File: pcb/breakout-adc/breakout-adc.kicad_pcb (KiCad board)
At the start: 4 copper layers, 100 x 62 mm, 107 parts, among them J1 Screw_Terminal_01x04, J10 Conn_01x01_Pin, J11 Conn_01x12_Pin, J12 Conn_01x12_Pin, J13 Conn_01x01_Pin, J14 Conn_01x01_Pin, J15 FX18-120P-0.8SV20, J16 Conn_01x01_Pin, J17 Conn_01x01_Pin, J18 Conn_01x01_Pin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

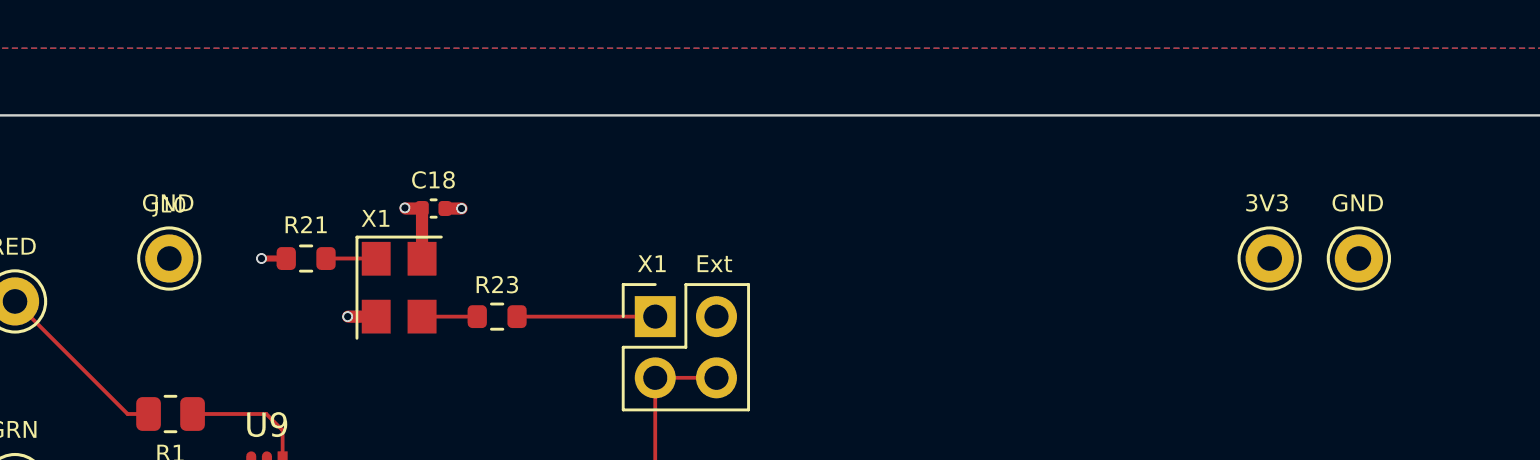
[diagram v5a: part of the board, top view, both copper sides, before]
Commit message: [adc][pcb] move the 3v3 and gnd tp to the edge
This will (probably) allow for grabbers to connect
to the through holes even if the tp isn't soldered in.
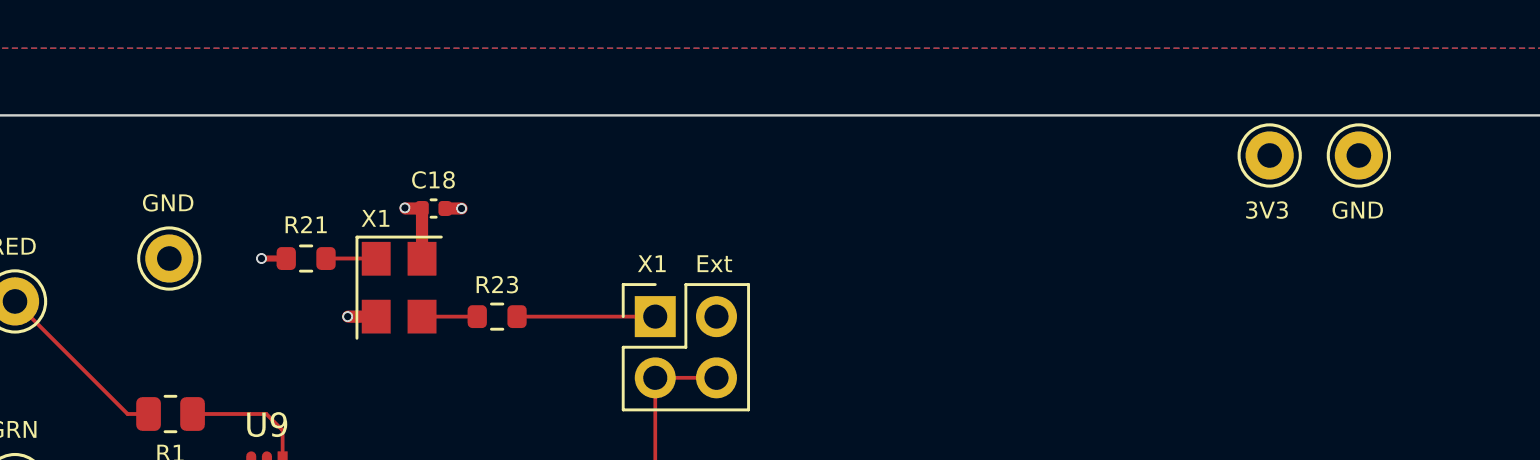
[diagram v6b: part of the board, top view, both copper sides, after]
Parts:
- moved J13 4.27 mm to (176.3, 45.2)
- moved J14 4.27 mm to (180.1, 45.2)
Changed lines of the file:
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@@
 	(footprint "keystone:KEYSTONE_5000"
 		(layer "F.Cu")
-		(at 176.35 49.475)
+		(at 176.35 45.2)
 		(property "Reference" "J13"
 			(at 0.032 -2.2064 0)
@@
 			(at 0.032 -2.2064 0)
 			(layer "F.SilkS")
+			(hide yes)
 			(effects
 				(font
@@
 	(footprint "keystone:KEYSTONE_5001"
 		(layer "F.Cu")
-		(at 180.05 49.475)
+		(at 180.05 45.2)
 		(property "Reference" "J14"
 			(at 0.032 -2.2064 0)
@@
 	)
 	(gr_text "GND"
-		(at 178.903334 47.6 0)
+		(at 178.903334 47.9 0)
 		(layer "F.SilkS")
 		(effects
@@
 	)
 	(gr_text "3V3"
-		(at 175.303333 47.6 0)
+		(at 175.303333 47.9 0)
 		(layer "F.SilkS")
 		(effects

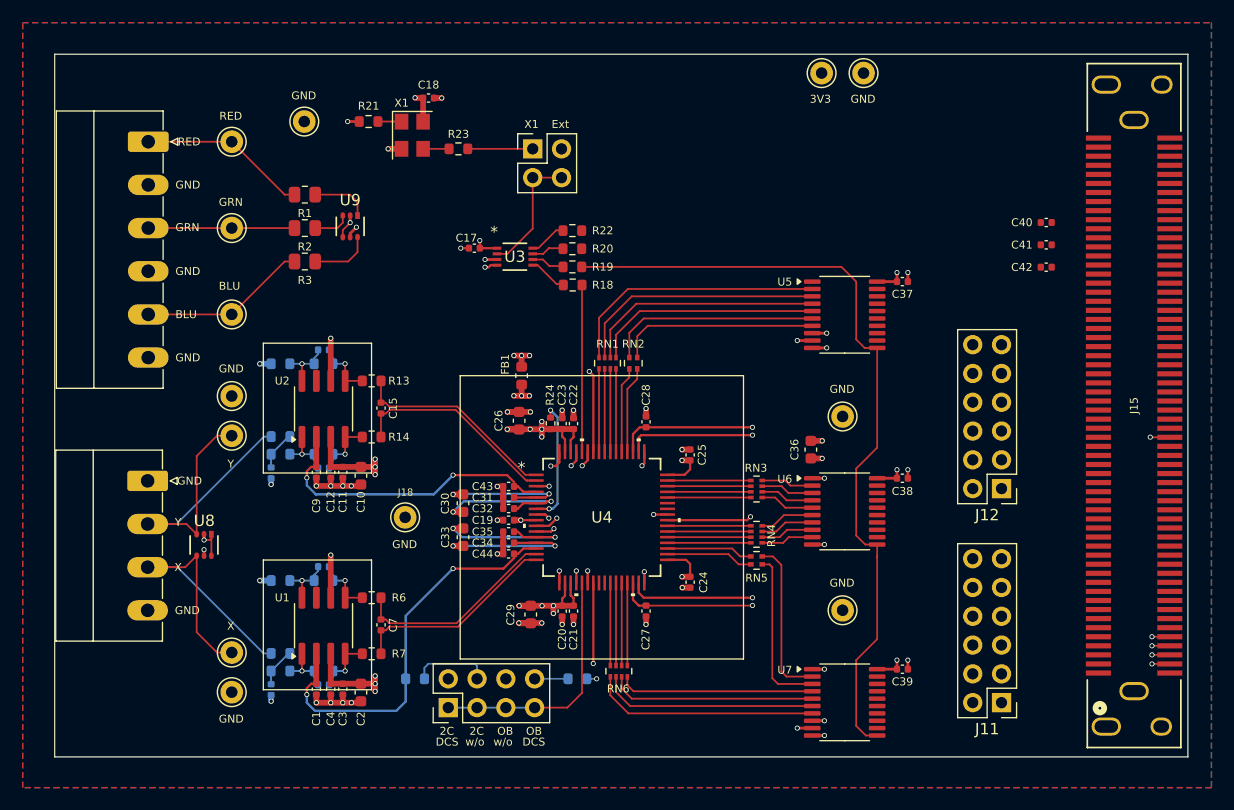
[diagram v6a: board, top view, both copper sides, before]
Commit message: [adc][pcb] routed data to buffers
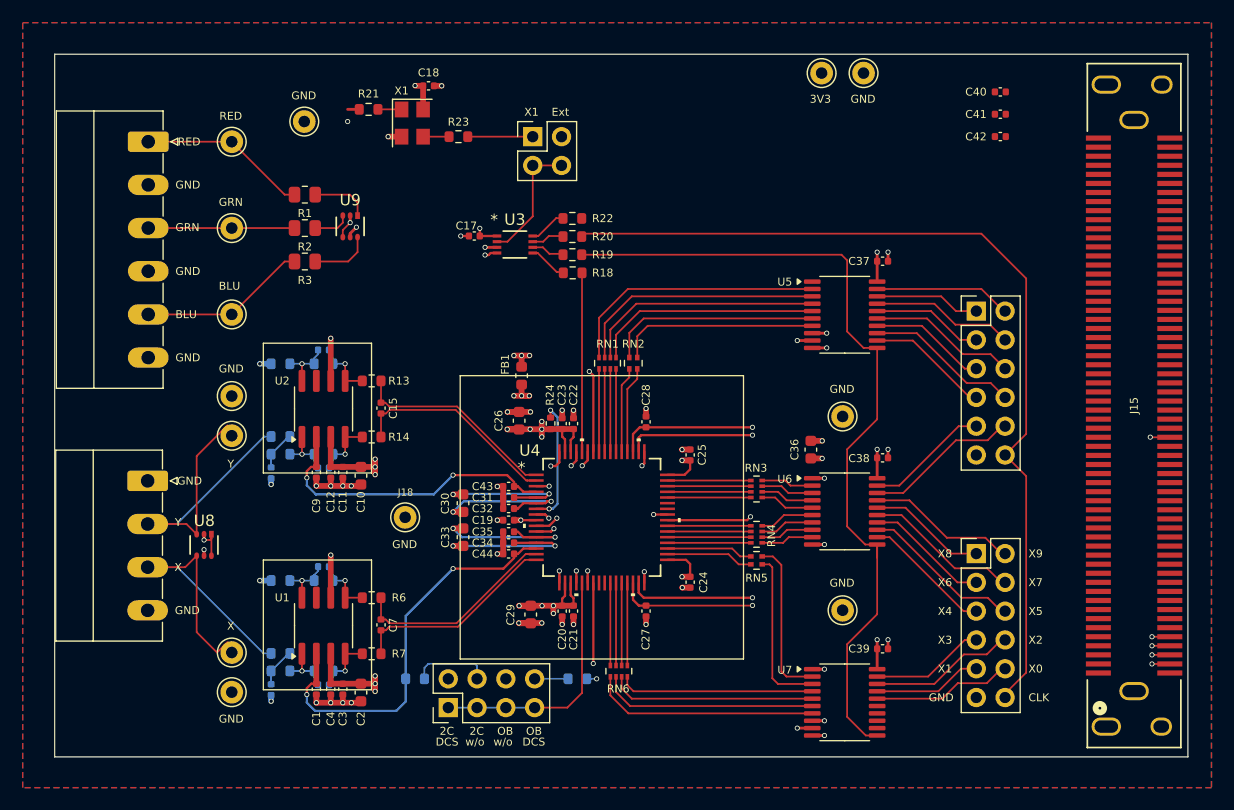
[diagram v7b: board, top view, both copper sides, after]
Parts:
- moved J12 15.8 mm to (190.0, 66.2), turned to 0 degrees
- moved J11 13.3 mm to (190.0, 87.6), turned to 0 degrees
- moved C42 12.2 mm to (192.1, 50.8)
- moved C40 12.2 mm to (192.1, 46.9)
- moved C41 12.2 mm to (192.1, 48.8)
- moved C37 2.51 mm to (181.7, 61.8)
- moved C38 2.51 mm to (181.7, 79.2)
- moved C39 2.51 mm to (181.7, 96.0)
- moved C17 1.08 mm to (145.7, 59.6)
- moved R20 1.08 mm to (154.4, 59.6)
- moved R21 1.08 mm to (136.4, 48.4)
- moved R22 1.08 mm to (154.4, 58.0)
- moved R23 1.08 mm to (144.3, 50.8)
- moved C18 1.07 mm to (141.7, 46.3)
- moved J20 1.07 mm to (150.9, 50.8)
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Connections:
- J11 pad 1: /X0 -> /X8
- J11 pad 10: /X9 -> /X0
- J11 pad 11: /ADC_CLK_HDR -> GND
- J11 pad 12: GND -> /ADC_CLK_HDR
- J11 pad 2: /X1 -> /X9
- J11 pad 3: /X2 -> /X6
- J11 pad 4: /X3 -> /X7
- J11 pad 7: /X6 -> /X3
- J11 pad 8: /X7 -> /X2
- J11 pad 9: /X8 -> /X1
- J12 pad 1: /Y0 -> /Y8
- J12 pad 10: /Y9 -> /Y0
- J12 pad 11: /ADC_CLK_HDR -> GND
- J12 pad 12: GND -> /ADC_CLK_HDR
- J12 pad 2: /Y1 -> /Y9
- J12 pad 3: /Y2 -> /Y6
- J12 pad 4: /Y3 -> /Y7
- J12 pad 7: /Y6 -> /Y2
- J12 pad 8: /Y7 -> /Y3
- J12 pad 9: /Y8 -> /Y1
- J3 pad 1: (no net) -> /X
- J4 pad 1: (no net) -> /Y
- R20 pad 1: /ADC_CLK_FPGA -> /ADC_CLK_HDR
- R22 pad 1: /ADC_CLK_HDR -> /ADC_CLK_FPGA
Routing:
- net /ADC_CLK_HDR: track 0.00 -> 80.4 mm
- net /X5: track 0.00 -> 13.9 mm
- net /Y0: track 0.00 -> 13.7 mm
- net /Y3: track 0.00 -> 13.6 mm
- net /X7: track 0.00 -> 13.4 mm
- net /X9: track 0.00 -> 13.2 mm
- net /Y5: track 0.00 -> 13.1 mm
- net /X2: track 0.00 -> 12.9 mm
- net /Y7: track 1.59 -> 14.2 mm
- net /Y9: track 1.66 -> 13.8 mm
- net /X0: track 0.00 -> 12.0 mm
- net /X4: track 0.00 -> 11.1 mm
- net /Y1: track 0.00 -> 10.9 mm
- net /Y2: track 0.00 -> 10.8 mm
- net /X6: track 0.00 -> 10.6 mm
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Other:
- board text added: "CLK"
- board text added: "X0"
- board text added: "X2"
- board text added: "X3"
- board text added: "X4"
- board text added: "X5"
- board text added: "X6"
- board text added: "X7"
- board text added: "X8"
- board text added: "X9"

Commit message: [pcb] add FX18-120P footprint and update pcbs
and a few adc fixes, including a key resistor fix
(the op amp for Y had a copy paste error from X
on the positive Rg)
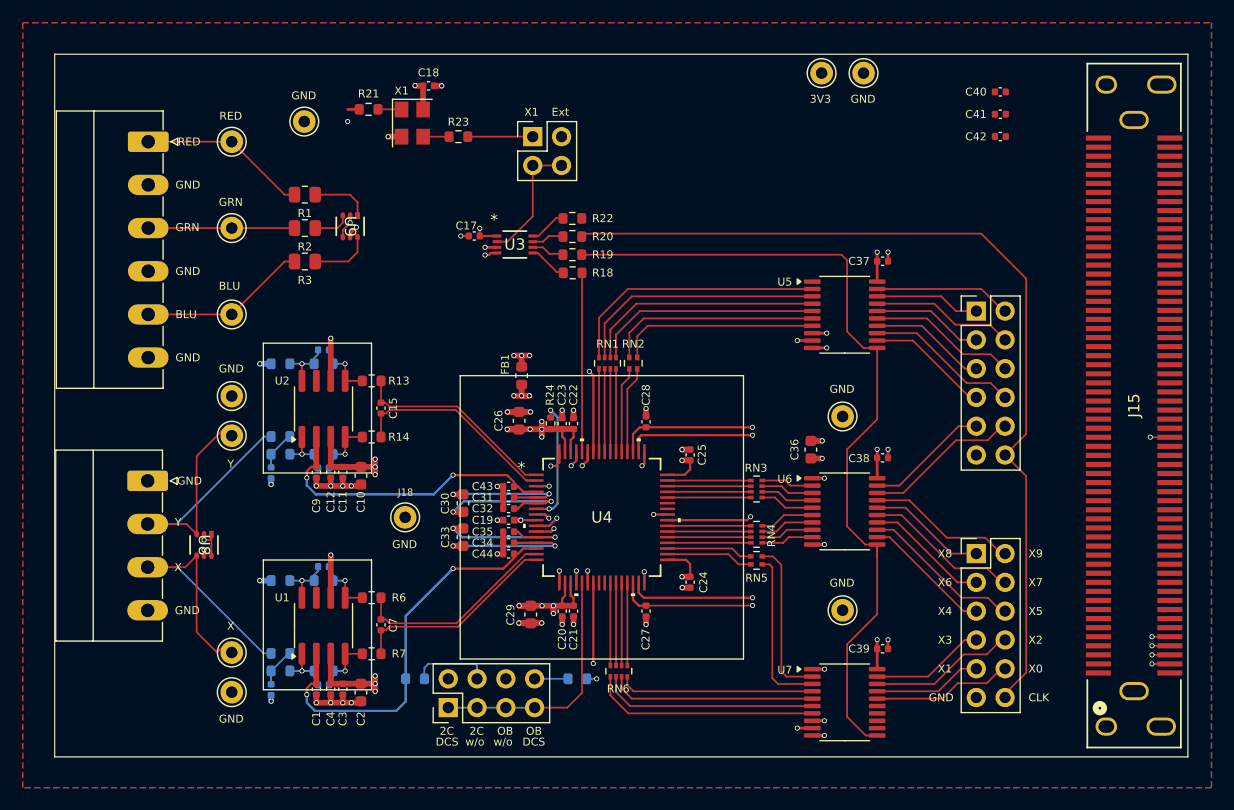
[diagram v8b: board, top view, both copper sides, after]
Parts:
- J15: footprint custom:CUSTOM_FX_120S-0.8SH20 -> custom:CUSTOM_FX_120P-0.8SH20
- R12: value 2.4k -> 1.8k
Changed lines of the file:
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@@
 		(tags "ADC10DL065CIVS/NOPB ")
 		(property "Reference" "U4"
-			(at -6.356666 -5.9 0)
+			(at 0 0 0)
 			(unlocked yes)
 			(layer "F.SilkS")
@@
 			)
 		)
-		(property "Footprint" "ADC10DL065:VEC64A_TEX"
+		(property "Footprint" "VEC64A_TEX"
 			(at 0 0 0)
 			(layer "F.Fab")
@@
 		(fp_text user "*"
 			(at -7.0866 -4.381 0)
-			(unlocked yes)
 			(layer "F.SilkS")
 			(effects
@@
 			)
 		)
-		(fp_text user "${REFERENCE}"
-			(at 0 0 0)
+		(fp_text user "*"
+			(at -4.6228 -3.619 0)
 			(unlocked yes)
 			(layer "F.Fab")
@@
 			)
 		)
-		(fp_text user "*"
-			(at -4.6228 -3.619 0)
+		(fp_text user "${REFERENCE}"
+			(at 0 0 0)
+			(unlocked yes)
 			(layer "F.Fab")
 			(effects
@@
 		(tags "Through hole pin header THT 2x06 2.54mm double row")
 		(property "Reference" "J11"
-			(at 1.27 -2.33 360)
+			(at 1.27 -2.33 0)
 			(layer "F.SilkS")
 			(hide yes)
@@
 		)
 		(property "Value" "Conn_01x12_Pin"
-			(at 1.270001 15.03 360)
+			(at 1.270001 15.03 0)
 			(layer "F.Fab")
 			(effects
@@
 			)
 		)
-		(property "Datasheet" "https://www.ti.com/lit/ds/scas301r/scas301r.pdf"
+		(property "Datasheet" "https://www.ti.com/lit/ds/symlink/sn74als574b.pdf"
 			(at 0 0 0)
 			(unlocked yes)
@@
 		(tags "D1213A-04S-7 ")
 		(property "Reference" "U8"
-			(at -2.14 -0.020491 0)
+			(at 0 0 -90)
 			(unlocked yes)
 			(layer "F.SilkS")
@@
 			)
 		)
-		(property "Footprint" "D1213A:SOT-363_DIO"
-			(at 0 0 90)
+		(property "Footprint" "SOT-363_DIO"
+			(at 0 0 -90)
 			(layer "F.Fab")
 			(hide yes)
@@
 			)
 		)
-		(property "Datasheet" "https://www.diodes.com/assets/Datasheets/D1213A-04S.pdf"
-			(at 0 0 90)
+		(property "Datasheet" "D1213A-04S-7"
+			(at 0 0 -90)
 			(layer "F.Fab")
 			(hide yes)
@@
 		)
 		(property "Description" ""
-			(at 0 0 90)
+			(at 0 0 -90)
 			(layer "F.Fab")
 			(hide yes)
@@
 			)
 		)
-		(property "Datasheet" "https://www.ti.com/lit/ds/scas301r/scas301r.pdf"
+		(property "Datasheet" "https://www.ti.com/lit/ds/symlink/sn74als574b.pdf"
 			(at 0 0 0)
 			(unlocked yes)
@@
 			)
 		)
-		(property "Datasheet" "https://www.ti.com/lit/ds/scas301r/scas301r.pdf"
+		(property "Datasheet" "https://www.ti.com/lit/ds/symlink/sn74als574b.pdf"
 			(at 0 0 0)
 			(unlocked yes)
@@
 		(tags "D1213A-04S-7 ")
 		(property "Reference" "U9"
-			(at -2.325 0 0)
+			(at 0 0 -90)
 			(unlocked yes)
 			(layer "F.SilkS")
@@
 			)
 		)
-		(property "Footprint" "D1213A:SOT-363_DIO"
-			(at 0 0 90)
+		(property "Footprint" "SOT-363_DIO"
+			(at 0 0 -90)
 			(layer "F.Fab")
 			(hide yes)
@@
 			)
 		)
-		(property "Datasheet" "https://www.diodes.com/assets/Datasheets/D1213A-04S.pdf"
-			(at 0 0 90)
+		(property "Datasheet" "D1213A-04S-7"
+			(at 0 0 -90)
 			(layer "F.Fab")
 			(hide yes)
@@
 		)
 		(property "Description" ""
-			(at 0 0 90)
+			(at 0 0 -90)
 			(layer "F.Fab")
 			(hide yes)
@@
 		)
 	)
-	(footprint "custom:CUSTOM_FX_120S-0.8SH20"
+	(footprint "custom:CUSTOM_FX_120P-0.8SH20"
 		(layer "F.Cu")
 		(at 203.922158 74.536978 90)
@@
 			(effects
 				(font
-					(size 0.7 0.7)
-					(thickness 0.1)
+					(size 1 1)
+					(thickness 0.15)
 				)
 			)
@@
 			)
 		)
-		(property "Footprint" "custom:CUSTOM_FX_120S-0.8SH20"
+		(property "Footprint" "custom:CUSTOM_FX_120P-0.8SH20"
 			(at 0 0 90)
 			(unlocked yes)
@@
 			)
 		)
-		(property "Datasheet" "FX18-120P-0.8SV20"
+		(property "Datasheet" "https://www.hirose.com/en/product/document?clcode=CL0579-0020-7-00&productname=FX18-120P-0.8SV&series=FX18&documenttype=2DDrawing&lang=en&documentid=0000920405"
 			(at 0 0 90)
 			(unlocked yes)
@@
 		)
 		(pad "121" thru_hole oval
-			(at -28.325 2.4 180)
+			(at -28.325 -2.45 180)
 			(size 1.908 1.608)
 			(drill oval 1.4 1.1)
@@
 		)
 		(pad "122" thru_hole oval
-			(at -28.325 -2.45 180)
+			(at -28.325 2.4 180)
 			(size 2.608001 1.608)
 			(drill oval 2.1 1.1)
@@
 		)
 		(pad "125" thru_hole oval
-			(at 28.325 2.45 180)
+			(at 28.325 -2.45 180)
 			(size 1.908 1.608)
 			(drill oval 1.4 1.1)
@@
 		)
 		(pad "126" thru_hole oval
-			(at 28.325 -2.45 180)
+			(at 28.325 2.45 180)
 			(size 2.608001 1.608)
 			(drill oval 2.1 1.1)
@@
 			(pintype "passive")
 		)
-		(model "${KIPRJMOD}/models/ul_FX18-120S-0-8SV20/FX18-120S-0.8SH.stp"
+		(model "${KIPRJMOD}/../models/ul_FX18-120P-0-8SV20/FX18-120P-0.8SH.stp"
 			(offset
-				(xyz 0.4 -3 3)
+				(xyz 0.4 -16.5 3)
 			)
 			(scale
@@
 		(tags "74AVC9112DCH ")
 		(property "Reference" "U3"
-			(at 0 -2.2 0)
+			(at 0 0 0)
 			(unlocked yes)
 			(layer "F.SilkS")
@@
 			)
 		)
-		(property "Footprint" "74AVC9112:VSSOP8_SOT765-1_NEX"
+		(property "Footprint" "VSSOP8_SOT765-1_NEX"
 			(at 0 0 0)
 			(layer "F.Fab")
@@
 		(fp_text user "*"
 			(at -1.8288 -2.1724 0)
+			(unlocked yes)
 			(layer "F.SilkS")
 			(effects
@@
 		(fp_text user "*"
 			(at -0.8128 -0.9779 0)
+			(unlocked yes)
 			(layer "F.Fab")
 			(effects
@@
 			)
 		)
-		(property "Datasheet" "https://support.epson.biz/td/api/doc_check.php?dl=brief_SG-8101CE"
+		(property "Datasheet" "https://support.epson.biz/td/api/doc_check.php?mode=dl&lang=en&Parts=SG-8 002DC"
 			(at 0 0 -90)
 			(unlocked yes)
@@
 		(tags "Through hole pin header THT 2x06 2.54mm double row")
 		(property "Reference" "J12"
-			(at 1.27 -2.33 360)
+			(at 1.27 -2.33 0)
 			(layer "F.SilkS")
 			(hide yes)
@@
 		)
 		(property "Value" "Conn_01x12_Pin"
-			(at 1.270001 15.03 360)
+			(at 1.270001 15.03 0)
 			(layer "F.Fab")
 			(effects
@@
 			)
 		)
-		(property "Value" "2.4k"
+		(property "Value" "1.8k"
 			(at 0 -1.43 0)
 			(layer "B.Fab")
